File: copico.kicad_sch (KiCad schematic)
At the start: 53 parts, among them P1 CocoEdgeConnector, P10 Power Bus, P2 5V Data Bus, P3 3.3V Data Bus, P4 3.3V Address Bus, P5 Debug, U1 74LS133, U2 74LS06, U3 PicoW, U4 SN74LVC245A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

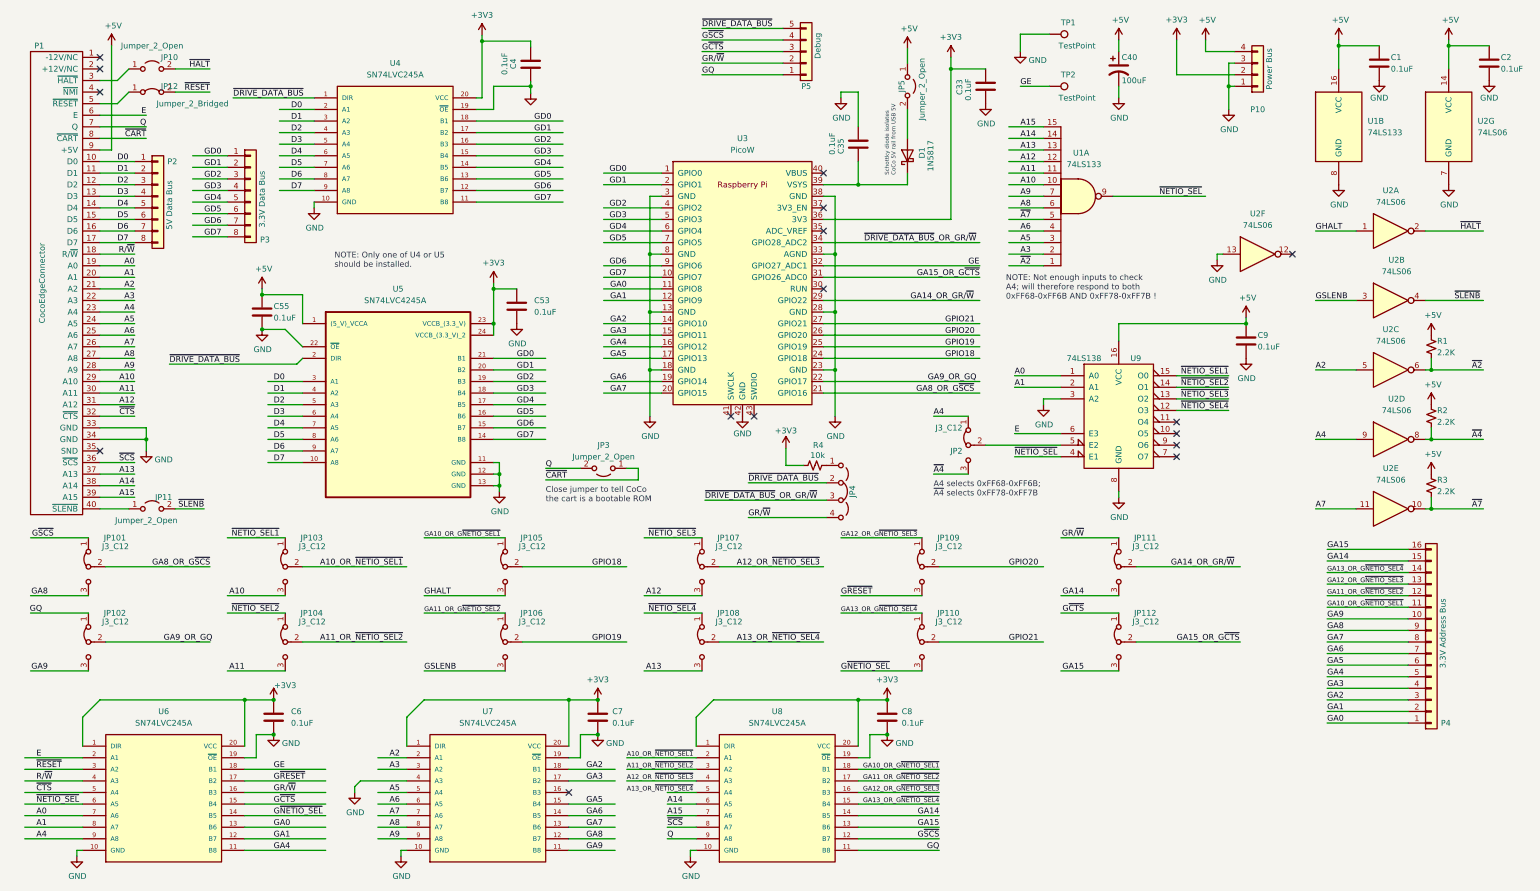
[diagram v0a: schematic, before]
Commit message: Update PCB layout with Rev 0.2 schematic changes
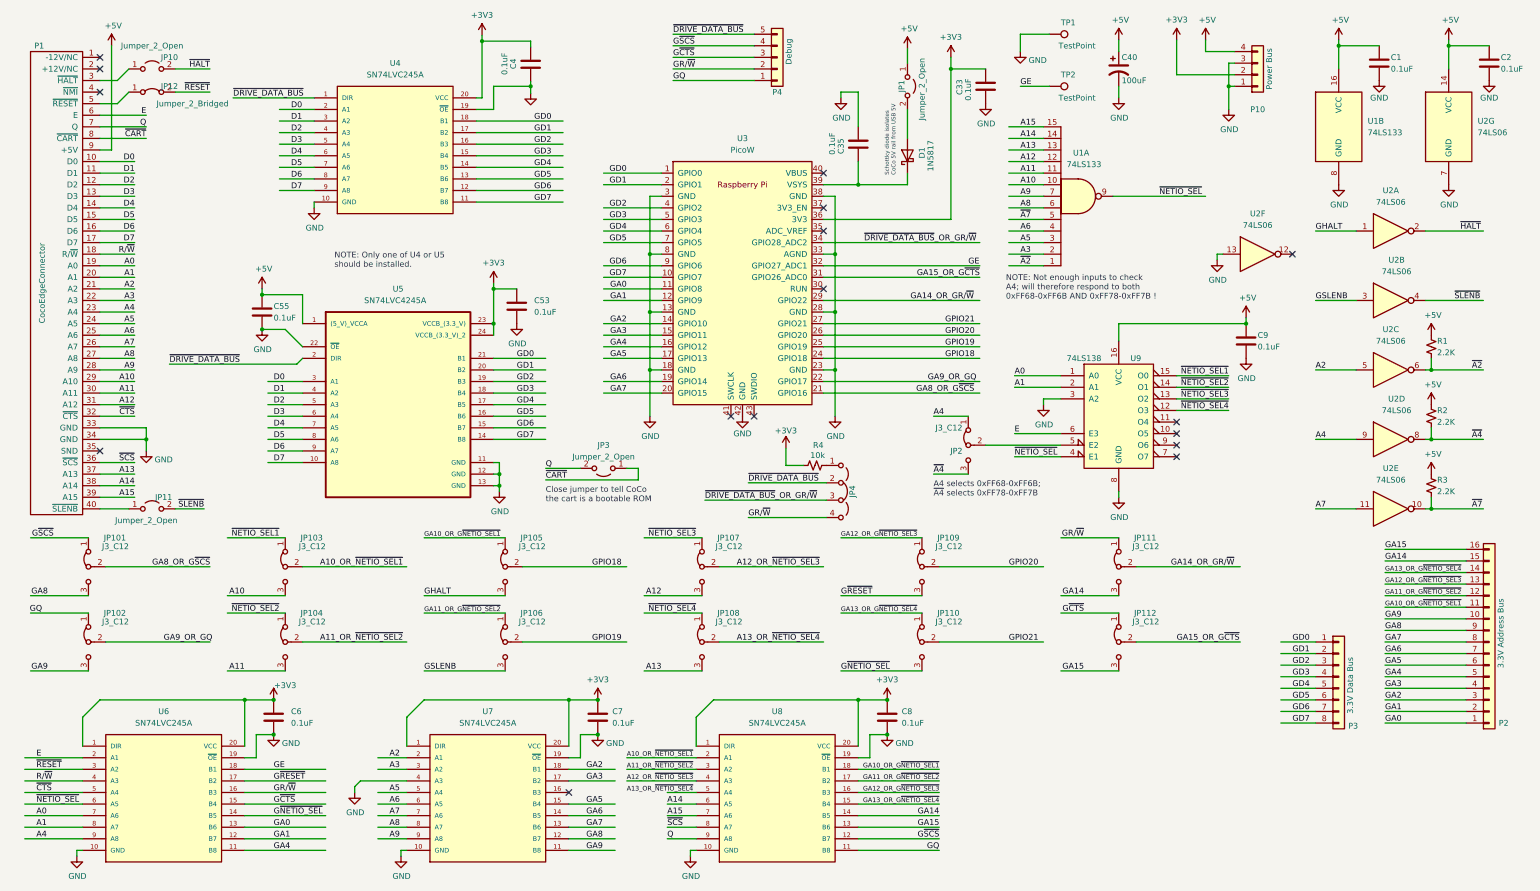
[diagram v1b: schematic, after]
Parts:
- removed P2: 5V Data Bus, Connector_PinHeader_2.54mm:PinHeader_1x08_P2.54mm_Vertical, symbol Connector_Generic:Conn_01x08
- renumbered JP5 to JP1, P4 to P2, P5 to P4
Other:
- company: Thomas Shanks (copico@tshanks.org) -> Thomas Shanks (copico@tshanks.org), Phoenix B (GitHub: phoenixvox), and contributors
- moved on the sheet: P2, P3, P4
